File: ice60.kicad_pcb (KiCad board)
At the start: 2 copper layers, 199 parts, among them J1 SWD, J2 JST SH 4-pin, SW0 SW_Push, SW1 MX_SW_solder, SW10 MX_SW_solder, SW11 MX_SW_solder, SW12 MX_SW_solder, SW13 MX_SW_solder, SW14 MX_SW_solder, SW15 MX_SW_solder, SW16 MX_SW_solder, SW17 MX_SW_solder, SW18 MX_SW_solder, SW19 MX_SW_solder, SW2 MX_SW_solder, SW20 MX_SW_solder, SW21 MX_SW_solder, SW22 MX_SW_solder, SW23 MX_SW_solder, SW24 MX_SW_solder, SW25 MX_SW_solder, SW26 MX_SW_solder, SW27 MX_SW_solder, SW28 MX_SW_solder, SW29 MX_SW_solder, SW3 MX_SW_solder, SW30 MX_SW_solder, SW31 MX_SW_solder, SW32 MX_SW_solder, SW33 MX_SW_solder, SW34 MX_SW_solder, SW35 MX_SW_solder, SW36 MX_SW_solder, SW37 MX_SW_solder, SW38 MX_SW_solder, SW39 MX_SW_solder, SW4 MX_SW_solder, SW40 MX_SW_solder, SW41 MX_SW_solder, SW42 MX_SW_solder, SW43 MX_SW_solder, SW44 MX_SW_solder, SW45 MX_SW_solder, SW46 MX_SW_solder, SW47 MX_SW_solder, SW48 MX_SW_solder, SW49 MX_SW_solder, SW5 MX_SW_solder, SW50 MX_SW_solder, SW51 MX_SW_solder, SW52 MX_SW_solder, SW53 MX_SW_solder, SW54 MX_SW_solder, SW55 MX_SW_solder, SW56 MX_SW_solder, SW57 MX_SW_solder, SW58 MX_SW_solder, SW59 MX_SW_solder, SW6 MX_SW_solder, SW60 MX_SW_solder, SW61 MX_SW_solder, SW62 MX_SW_solder, SW63 MX_SW_solder, SW64 MX_SW_solder, SW65 MX_SW_solder, SW66 MX_SW_solder, SW67 MX_SW_solder, SW68 MX_SW_solder, SW69 MX_SW_solder, SW7 MX_SW_solder, SW70 MX_SW_solder, SW71 MX_SW_solder, SW72 MX_SW_solder, SW73 MX_SW_solder, SW74 MX_SW_solder, SW75 MX_SW_solder, SW76 MX_SW_solder, SW77 MX_SW_solder, SW78 MX_SW_solder, SW79 MX_SW_solder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

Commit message: flip some switches to simplify routing
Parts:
- D1, D10, D11, D12, D13, D14, D16, D17, D18, D19, D2, D20, D21, D22, D23, D24, D25, D26, D27, D28, D29, D3, D32, D33, D34, D35, D36, D37, D38, D39, D4, D40, D41, D42, D43, D44, D46, D48, D49, D5, D50, D51, D52, D53, D54, D55, D56, D57, D58, D59, D6, D60, D62, D63, D65, D68, D7, D71, D73, D77, D8, D80, D81, D84, D87, D9: moved to B.Cu
- moved D2 493.9 mm to (52.4, -11.9), turned to 90 degrees
- moved D1 491.8 mm to (35.7, -11.9), turned to 90 degrees
- moved D29 178.1 mm to (595.3, 185.6), turned to 90 degrees
- moved D14 27.9 mm to (543.4, 53.5), turned to 90 degrees
- moved D54 27.7 mm to (577.1, 20.0), turned to 90 degrees
- moved D46 27.3 mm to (499.7, 97.6), turned to 90 degrees
- moved D65 27.3 mm to (519.9, 77.4), turned to 90 degrees
- moved D28 26.7 mm to (469.5, 128.3), turned to 90 degrees
- moved D24 26.5 mm to (563.6, 34.3), turned to 90 degrees
- moved D81 26.3 mm to (583.8, 14.3), turned to 90 degrees
- moved D7 26.1 mm to (439.2, 159.0), turned to 90 degrees
- moved D8 26.1 mm to (459.4, 138.8), turned to 90 degrees
- moved D4 25.3 mm to (476.2, 122.5), turned to 90 degrees
- moved D80 25.3 mm to (509.9, 88.9), turned to 90 degrees
- moved D18 24.8 mm to (445.9, 153.2), turned to 90 degrees
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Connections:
- SW10 pad 1: COL09 -> Net-(D10-Pad2)
- SW10 pad 2: Net-(D10-Pad2) -> COL09
- SW11 pad 1: COL10 -> Net-(D11-Pad2)
- SW11 pad 2: Net-(D11-Pad2) -> COL10
- SW12 pad 1: COL11 -> Net-(D12-Pad2)
- SW12 pad 2: Net-(D12-Pad2) -> COL11
- SW13 pad 1: COL12 -> Net-(D13-Pad2)
- SW13 pad 2: Net-(D13-Pad2) -> COL12
- SW2 pad 1: COL01 -> Net-(D2-Pad2)
- SW2 pad 2: Net-(D2-Pad2) -> COL01
- SW3 pad 1: COL02 -> Net-(D3-Pad2)
- SW3 pad 2: Net-(D3-Pad2) -> COL02
- SW4 pad 1: COL03 -> Net-(D4-Pad2)
- SW4 pad 2: Net-(D4-Pad2) -> COL03
- SW49 pad 1: COL01 -> Net-(D49-Pad2)
- SW49 pad 2: Net-(D49-Pad2) -> COL01
- SW5 pad 1: COL04 -> Net-(D5-Pad2)
- SW5 pad 2: Net-(D5-Pad2) -> COL04
- SW50 pad 1: COL02 -> Net-(D50-Pad2)
- SW50 pad 2: Net-(D50-Pad2) -> COL02
- SW51 pad 1: COL03 -> Net-(D51-Pad2)
- SW51 pad 2: Net-(D51-Pad2) -> COL03
- SW52 pad 1: COL04 -> Net-(D52-Pad2)
- SW52 pad 2: Net-(D52-Pad2) -> COL04
- SW53 pad 1: COL05 -> Net-(D53-Pad2)
- SW53 pad 2: Net-(D53-Pad2) -> COL05
- SW54 pad 1: COL06 -> Net-(D54-Pad2)
- SW54 pad 2: Net-(D54-Pad2) -> COL06
- SW55 pad 1: COL07 -> Net-(D55-Pad2)
- SW55 pad 2: Net-(D55-Pad2) -> COL07
- SW56 pad 1: COL08 -> Net-(D56-Pad2)
- SW56 pad 2: Net-(D56-Pad2) -> COL08
- SW57 pad 1: COL09 -> Net-(D57-Pad2)
- SW57 pad 2: Net-(D57-Pad2) -> COL09
- SW58 pad 1: COL10 -> Net-(D58-Pad2)
- SW58 pad 2: Net-(D58-Pad2) -> COL10
- SW59 pad 1: COL11 -> Net-(D59-Pad2)
- SW59 pad 2: Net-(D59-Pad2) -> COL11
- SW6 pad 1: COL05 -> Net-(D6-Pad2)
- SW6 pad 2: Net-(D6-Pad2) -> COL05
- SW7 pad 1: COL06 -> Net-(D7-Pad2)
- SW7 pad 2: Net-(D7-Pad2) -> COL06
- SW71 pad 1: COL05 -> Net-(D71-Pad2)
- SW71 pad 2: Net-(D71-Pad2) -> COL05
- SW72 pad 1: COL05 -> Net-(D71-Pad2)
- SW72 pad 2: Net-(D71-Pad2) -> COL05
- SW8 pad 1: COL07 -> Net-(D8-Pad2)
- SW8 pad 2: Net-(D8-Pad2) -> COL07
- SW80 pad 1: COL10 -> Net-(D80-Pad2)
- SW80 pad 2: Net-(D80-Pad2) -> COL10
- SW9 pad 1: COL08 -> Net-(D9-Pad2)
- SW9 pad 2: Net-(D9-Pad2) -> COL08

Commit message: preliminary diode placement
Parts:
- moved D17 523.6 mm to (64.3, 42.9), turned to -90 degrees
- moved D50 519.7 mm to (64.3, 81.0), turned to -90 degrees
- moved D32 497.2 mm to (42.9, 61.9), turned to -90 degrees
- moved D16 470.6 mm to (40.5, 42.9), turned to -90 degrees
- moved D63 462.6 mm to (40.5, 100.0), turned to -90 degrees
- moved D65 456.1 mm to (64.3, 97.6), turned to -90 degrees
- moved D48 445.4 mm to (23.8, 81.0), turned to -90 degrees
- moved D54 440.8 mm to (140.5, 81.0), turned to -90 degrees
- moved D35 439.6 mm to (107.2, 61.9), turned to -90 degrees
- moved D33 439.3 mm to (69.1, 61.9), turned to -90 degrees
- moved D6 436.1 mm to (131.0, 23.8), turned to -90 degrees
- moved D51 429.9 mm to (83.3, 81.0), turned to -90 degrees
- moved D49 429.3 mm to (59.5, 81.0), turned to -90 degrees
- moved D3 422.8 mm to (73.8, 23.8), turned to -90 degrees
- moved D5 418.9 mm to (111.9, 23.8), turned to -90 degrees
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
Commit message: tweak diodes
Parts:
- moved D46 29.1 mm to (278.6, 40.5)
- moved D32 19.2 mm to (23.8, 59.5)
- moved D28 14.5 mm to (259.6, 40.5)
- moved D12 14.3 mm to (231.0, 23.8)
- moved D13 14.3 mm to (250.0, 23.8)
- moved D7 14.3 mm to (135.7, 23.8)
- moved D4 14.3 mm to (78.6, 23.8)
- moved D5 14.3 mm to (97.6, 23.8)
- moved D10 14.3 mm to (192.9, 23.8)
- moved D11 14.3 mm to (211.9, 23.8)
- moved D2 14.3 mm to (40.5, 23.8)
- moved D3 14.3 mm to (59.5, 23.8)
- moved D6 14.3 mm to (116.7, 23.8)
- moved D8 14.3 mm to (154.8, 23.8)
- moved D9 14.3 mm to (173.8, 23.8)
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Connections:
- SW14 pad 1: COL13 -> Net-(D14-Pad2)
- SW14 pad 2: Net-(D14-Pad2) -> COL13
- SW15 pad 1: COL13 -> Net-(D14-Pad2)
- SW15 pad 2: Net-(D14-Pad2) -> COL13
- SW28 pad 1: COL12 -> Net-(D28-Pad2)
- SW28 pad 2: Net-(D28-Pad2) -> COL12
- SW29 pad 1: COL13 -> Net-(D29-Pad2)
- SW29 pad 2: Net-(D29-Pad2) -> COL13
- SW30 pad 1: COL13 -> Net-(D29-Pad2)
- SW30 pad 2: Net-(D29-Pad2) -> COL13
- SW31 pad 1: COL00 -> Net-(D32-Pad2)
- SW31 pad 2: Net-(D32-Pad2) -> COL00
- SW32 pad 1: COL00 -> Net-(D32-Pad2)
- SW32 pad 2: Net-(D32-Pad2) -> COL00
- SW47 pad 1: COL00 -> Net-(D48-Pad2)
- SW47 pad 2: Net-(D48-Pad2) -> COL00
- SW48 pad 1: COL00 -> Net-(D48-Pad2)
- SW48 pad 2: Net-(D48-Pad2) -> COL00
- SW60 pad 1: COL12 -> Net-(D60-Pad2)
- SW60 pad 2: Net-(D60-Pad2) -> COL12
- SW61 pad 1: COL12 -> Net-(D60-Pad2)
- SW61 pad 2: Net-(D60-Pad2) -> COL12
- SW62 pad 1: COL13 -> Net-(D62-Pad2)
- SW62 pad 2: Net-(D62-Pad2) -> COL13
- SW80 pad 1: Net-(D80-Pad2) -> COL10
- SW80 pad 2: COL10 -> Net-(D80-Pad2)
- SW87 pad 1: COL13 -> Net-(D87-Pad2)
- SW87 pad 2: Net-(D87-Pad2) -> COL13
- SW88 pad 1: COL13 -> Net-(D87-Pad2)
- SW88 pad 2: Net-(D87-Pad2) -> COL13

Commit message: preliminary SMD component placements
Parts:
- C1, C10, C11, C12, C13, C14, C15, C16, C17, C2, C3, C4, C5, C6, C7, C8, C9, F1, J1, J2, R1, R2, R3, R4, R5, SW0, U1, U2, U3, U4, Y1: moved to B.Cu
- moved R4 358.4 mm to (39.7, 64.8), turned to 90 degrees
- moved C1 354.5 mm to (43.5, 61.0), turned to 90 degrees
- moved C2 353.3 mm to (51.1, 48.3), turned to 90 degrees
- moved SW0 352.4 mm to (37.1, 57.1), turned to 180 degrees
- moved C15 347.3 mm to (54.9, 66.0), turned to 180 degrees
- moved C12 344.7 mm to (58.1, 62.7), turned to 90 degrees
- moved C11 344.0 mm to (54.9, 67.3), turned to 180 degrees
- moved C6 343.1 mm to (59.4, 62.2), turned to 90 degrees
- moved C3 343.0 mm to (54.9, 57.1), turned to 90 degrees
- moved R3 340.2 mm to (59.6, 53.3), turned to -90 degrees
- moved U3 339.8 mm to (54.9, 53.3), turned to 90 degrees
- moved C16 338.5 mm to (56.8, 63.5), turned to 90 degrees
- moved C17 337.8 mm to (58.1, 71.1), turned to -90 degrees
- moved C7 337.6 mm to (54.9, 64.8), turned to 180 degrees
- moved R2 334.8 mm to (61.3, 53.3), turned to -90 degrees
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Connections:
- D16 pad 2: Net-(D16-Pad2) -> Net-(SW16-Pad1)
- J1 pad 3: GND -> SWD
- J1 pad 4: SWD -> GND
- SW16 pad 1: COL00 -> Net-(SW16-Pad1)
- SW16 pad 2: Net-(D16-Pad2) -> COL00
- U4 pad 3: D_N -> D_P
- U4 pad 5: +5V -> VBUS
- U4 pad 6: D_P -> D_N

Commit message: improve footprint positions
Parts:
- moved J1 58.3 mm to (42.5, 85.1), turned to -90 degrees
- moved R1 57.1 mm to (43.1, 81.3), turned to 180 degrees
- moved SW0 48.5 mm to (76.8, 85.1), turned to 90 degrees
- moved D43 36.7 mm to (73.5, 100.3)
- moved C1 32.1 mm to (74.3, 69.8), turned to 180 degrees
- moved R4 30.7 mm to (66.7, 79.5)
- moved U2 29.6 mm to (76.8, 64.8), turned to 0 degrees
- moved C9 14.2 mm to (62.9, 75.4), turned to -90 degrees
- moved C16 13.4 mm to (70.0, 66.0), turned to 0 degrees
- moved C8 12.9 mm to (55.2, 75.4), turned to -90 degrees
- moved C12 12.8 mm to (70.0, 67.3), turned to 0 degrees
- moved C6 12.4 mm to (70.0, 68.6), turned to 0 degrees
- moved C10 12.2 mm to (70.0, 69.8), turned to 0 degrees
- moved C14 12.1 mm to (56.5, 75.4), turned to -90 degrees
- moved C17 9.38 mm to (57.8, 61.8), turned to 90 degrees
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- renumbered D16 to D15, D17 to D16, D18 to D17, D19 to D18, D20 to D19, D21 to D20, D22 to D21, D23 to D22, D24 to D23, D25 to D24, D26 to D25, D27 to D26, D28 to D27, D29 to D28, D32 to D29, D33 to D30, D34 to D31, D35 to D32, D36 to D33, D37 to D34, D38 to D35, D39 to D36, D40 to D37, D41 to D38, D42 to D39, D43 to D40, D44 to D41, D46 to D42, D48 to D43, D49 to D44, D50 to D45, D51 to D46, D52 to D47, D53 to D48, D54 to D49, D55 to D50, D56 to D51, D57 to D52, D58 to D53, D59 to D54, D60 to D55, D62 to D56, D63 to D57, D65 to D58, D68 to D59, D71 to D60, D73 to D61, D77 to D62, D80 to D63, D81 to D64, D84 to D65, D87 to D66
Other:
- board outline added: 284.8 x 94.2 mm

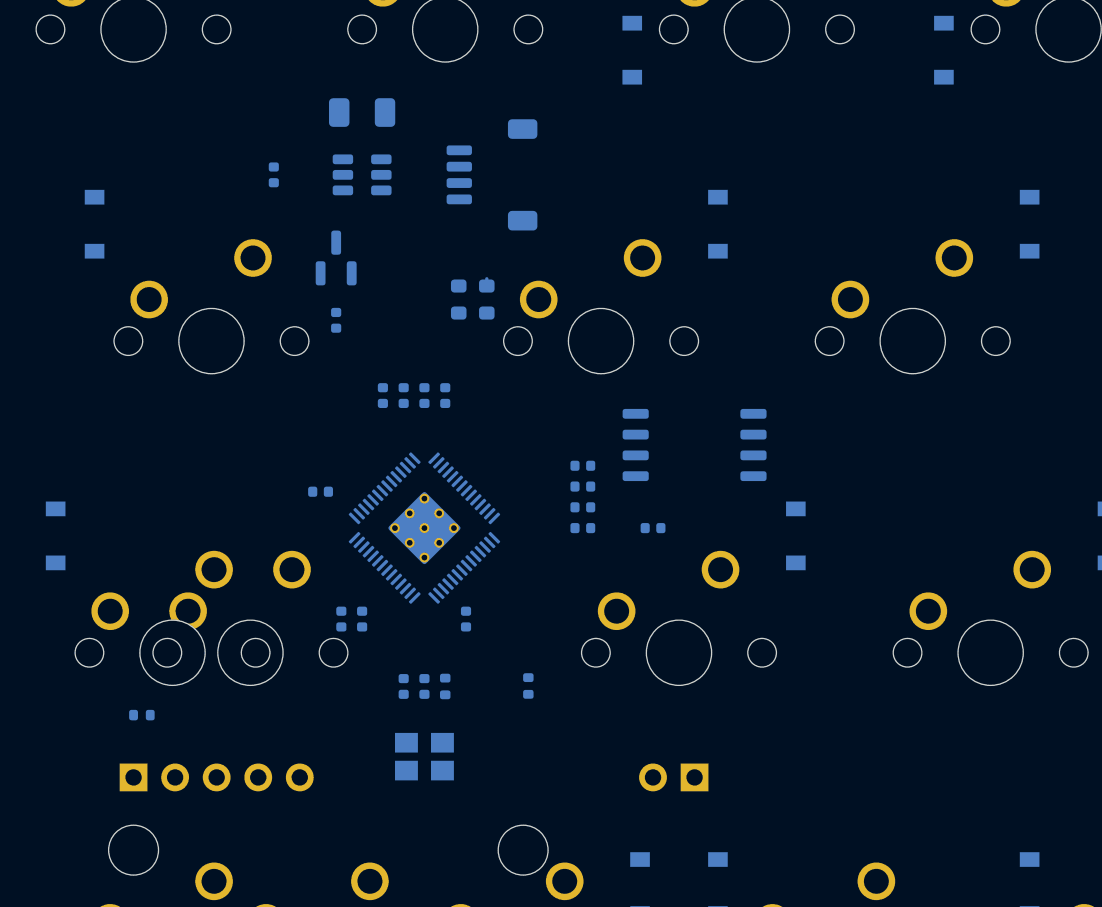
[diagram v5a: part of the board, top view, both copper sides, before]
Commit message: wire up most things other than matrix
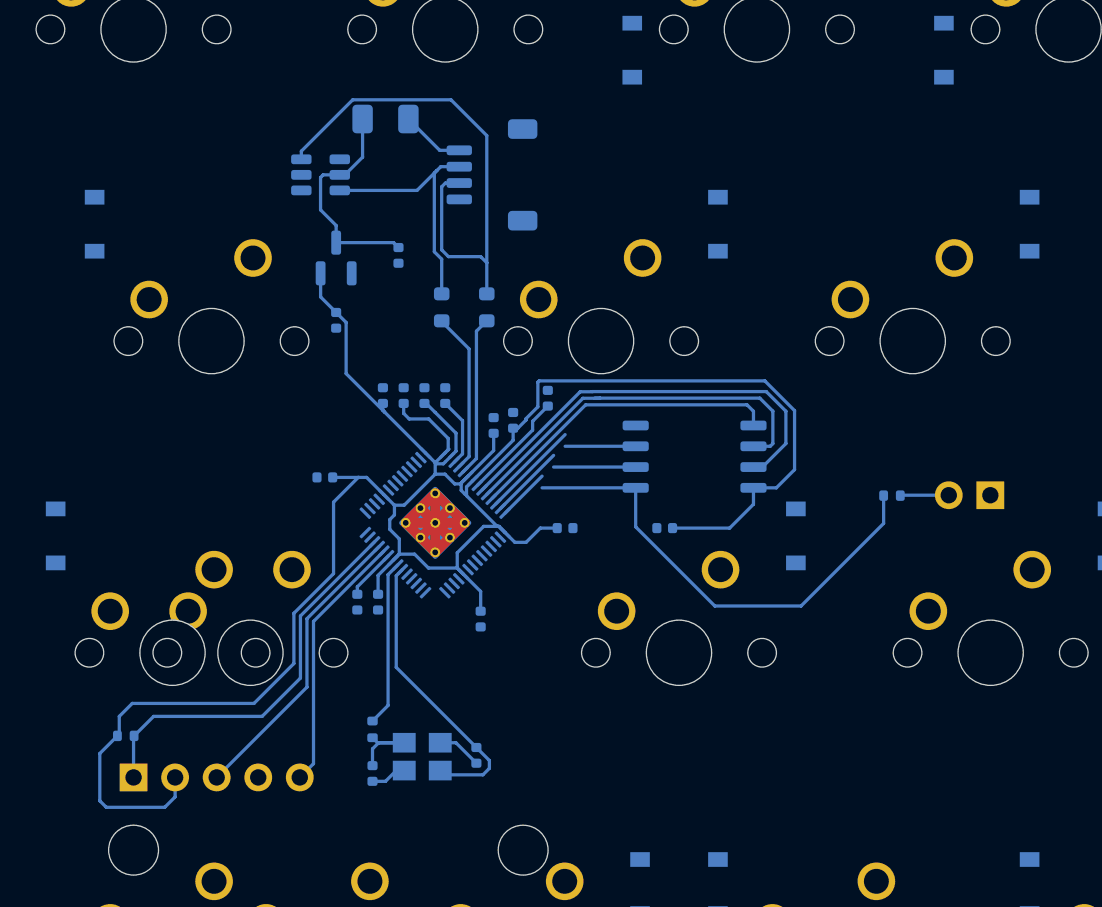
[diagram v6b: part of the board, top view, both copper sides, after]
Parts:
- moved R4 25.1 mm to (88.9, 67.9), turned to 180 degrees
- moved SW0 25.0 mm to (94.9, 67.8)
- moved C2 9.07 mm to (58.7, 53.2)
- moved C6 7.00 mm to (67.9, 61.9), turned to 90 degrees
- moved C5 6.19 mm to (57.1, 84.8), turned to 90 degrees
- moved C4 6.12 mm to (63.5, 83.7), turned to 90 degrees
- moved C16 5.98 mm to (64.6, 63.6), turned to 90 degrees
- moved C12 5.88 mm to (65.7, 63.3), turned to 90 degrees
- moved R5 5.16 mm to (57.1, 82.2)
- moved U4 2.54 mm to (54.0, 48.3), turned to 0 degrees
- moved R1 1.61 mm to (42.1, 82.5), turned to 0 degrees
- moved F1 1.48 mm to (57.9, 44.8)
- moved C14 1.42 mm to (57.5, 74.4)
- moved C8 1.42 mm to (56.2, 74.4)
- moved R3 1.14 mm to (61.4, 56.4)
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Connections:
- U4 pad 5: VBUS -> +5V
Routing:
- net +3V3: track 0.00 -> 143.2 mm
- net CS: track 0.00 -> 32.3 mm
- net D_P: track 0.45 -> 31.8 mm
- net GND: track 0.00 -> 27.5 mm
- net SD3: track 0.00 -> 26.1 mm
- net ~{RESET}: track 0.00 -> 24.4 mm
- net QSPI_CLK: track 0.00 -> 23.8 mm
- net SD0: track 0.00 -> 19.4 mm
- net SWD: track 0.00 -> 18.2 mm
- net XTAL_IN: track 0.00 -> 17.9 mm
- net SWCLK: track 0.00 -> 16.6 mm
- net D_N: track 0.00 -> 15.7 mm
- net +1V1: track 0.00 -> 14.0 mm
- net +5V: track 0.00 -> 13.7 mm
- net SD2: track 0.00 -> 10.3 mm
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
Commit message: route columns and row 0
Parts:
- moved J1 17.6 mm to (41.2, 67.6)
- moved R1 12.6 mm to (42.5, 69.9), turned to 180 degrees
- moved D15 5.56 mm to (45.7, 51.3)
- moved C13 1.97 mm to (56.0, 66.0), turned to 90 degrees
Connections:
- U1 pad 37: unconnected-(U1-Pad37) -> ROW0
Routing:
- net ROW0: track 0.00 -> 253.1 mm
- net COL12: track 0.00 -> 127.7 mm
- net COL08: track 0.00 -> 123.5 mm
- net COL00: track 0.00 -> 119.9 mm
- net COL06: track 0.00 -> 109.2 mm
- net COL11: track 0.00 -> 108.1 mm
- net COL05: track 0.00 -> 106.0 mm
- net COL13: track 0.00 -> 97.3 mm
- net COL01: track 0.00 -> 96.8 mm
- net COL02: track 0.00 -> 96.0 mm
- net COL10: track 0.00 -> 87.9 mm
- net COL03: track 0.00 -> 62.2 mm
- net COL07: track 0.00 -> 62.2 mm
- net COL04: track 0.00 -> 62.2 mm
- net COL09: track 0.00 -> 62.2 mm
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
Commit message: complete initial routing
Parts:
- moved D43 36.8 mm to (37.8, 91.7)
- moved D42 15.9 mm to (315.6, 46.5), turned to 90 degrees
- moved D29 15.7 mm to (47.6, 82.5), turned to 180 degrees
- moved D41 11.9 mm to (278.2, 70.2)
- moved D28 1.98 mm to (289.0, 55.2)
- moved C13 1.13 mm to (55.2, 66.7)
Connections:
- U1 pad 11: unconnected-(U1-Pad11) -> COL09
- U1 pad 12: unconnected-(U1-Pad12) -> COL10
- U1 pad 13: unconnected-(U1-Pad13) -> COL11
- U1 pad 14: unconnected-(U1-Pad14) -> COL12
- U1 pad 15: unconnected-(U1-Pad15) -> COL13
- U1 pad 2: unconnected-(U1-Pad2) -> ROW2
- U1 pad 3: unconnected-(U1-Pad3) -> COL02
- U1 pad 36: unconnected-(U1-Pad36) -> ROW3
- U1 pad 37: ROW0 -> ROW4
- U1 pad 38: unconnected-(U1-Pad38) -> ROW0
- U1 pad 39: unconnected-(U1-Pad39) -> COL01
- U1 pad 4: unconnected-(U1-Pad4) -> COL03
- U1 pad 40: unconnected-(U1-Pad40) -> COL00
- U1 pad 41: unconnected-(U1-Pad41) -> ROW1
- U1 pad 5: unconnected-(U1-Pad5) -> COL04
- U1 pad 6: unconnected-(U1-Pad6) -> COL05
- U1 pad 7: unconnected-(U1-Pad7) -> COL06
- U1 pad 8: unconnected-(U1-Pad8) -> COL07
- U1 pad 9: unconnected-(U1-Pad9) -> COL08
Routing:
- net ROW3: track 0.00 -> 334.5 mm
- net ROW4: track 0.00 -> 333.8 mm
- net ROW2: track 23.2 -> 310.6 mm, vias 0 -> 2
- net ROW1: track 0.00 -> 274.5 mm
- net COL13: track 97.3 -> 360.6 mm
- net COL12: track 127.7 -> 357.8 mm
- net COL11: track 108.1 -> 318.6 mm
- net COL10: track 87.9 -> 278.8 mm
- net COL09: track 62.2 -> 233.6 mm
- net COL08: track 123.5 -> 275.5 mm
- net COL07: track 62.2 -> 194.6 mm
- net COL06: track 109.2 -> 223.6 mm
- net COL05: track 106.0 -> 199.4 mm
- net COL04: track 62.2 -> 136.0 mm
- net COL01: track 96.8 -> 161.5 mm
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- added copper zone on B.Cu, net GND
- added copper zone on F.Cu, net GND
